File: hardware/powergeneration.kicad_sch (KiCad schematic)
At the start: 36 parts, among them U11 TPS55340PWPR, U5 AOZ1284PI, U6 TL431BIDBZR

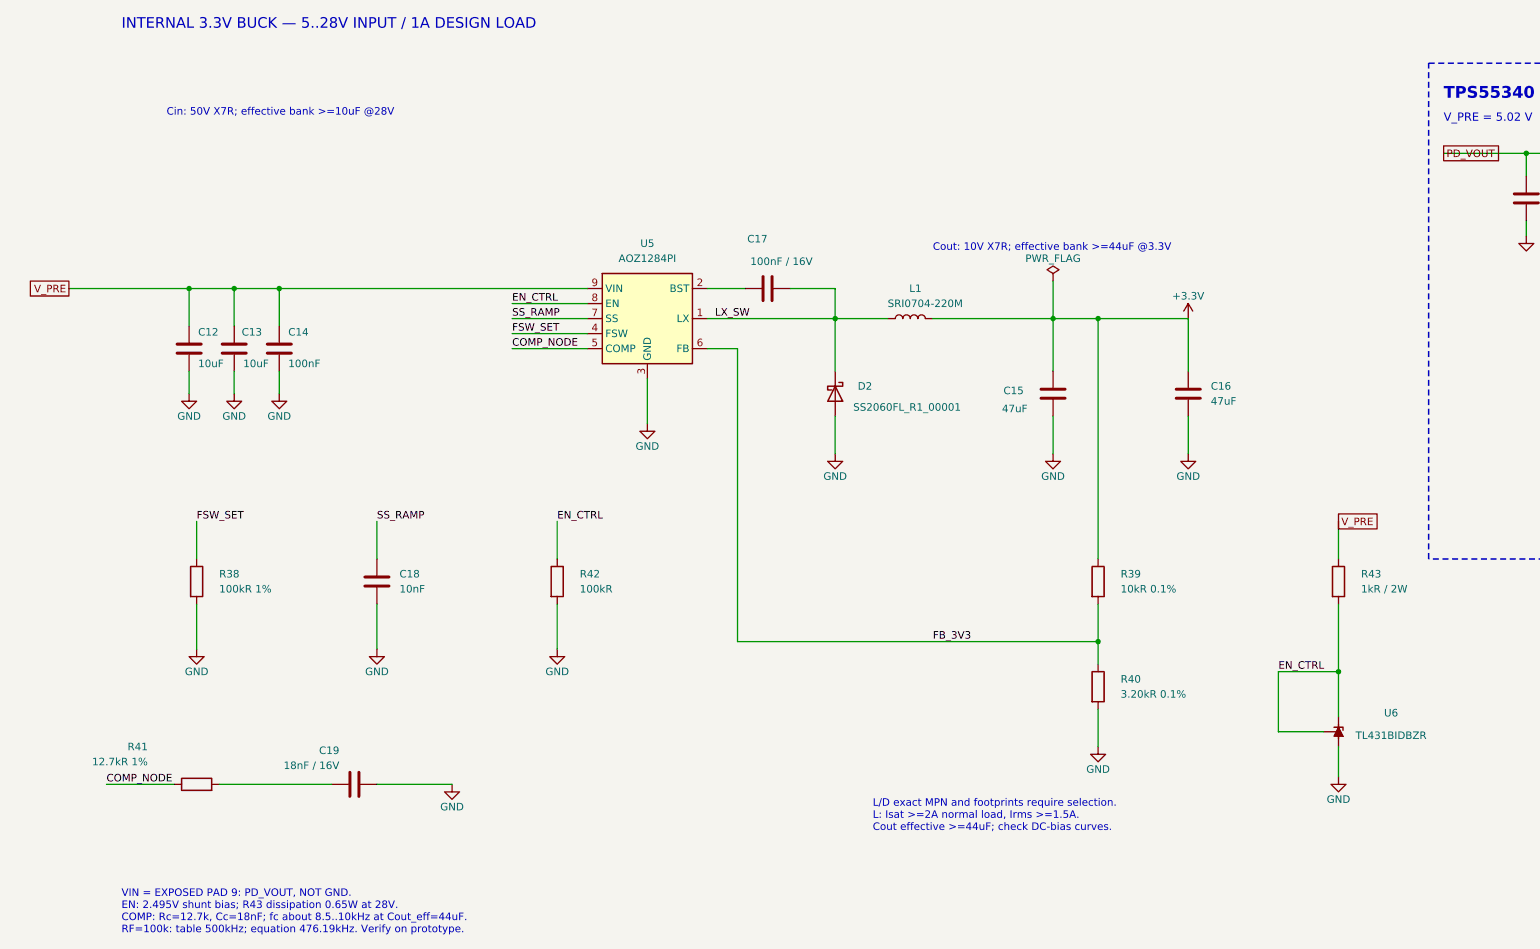
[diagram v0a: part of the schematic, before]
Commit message: powergeneration: AOZ1284 buck bölümünü telle yeniden çiz
Etiketle bağlanan pasifler (EN/TL431, SS, FSW, COMP, FB bölücü) IC
pinlerine gerçek tellerle bağlandı; blok çerçeve ve başlık aldı.
R38-R43 Device:R -> R_Small_US. VIN notu PD_VOUT değil V_PRE olarak
düzeltildi. Netlist değişmedi.

Co-Authored-By: Claude Opus 5 <noreply@anthropic.com>
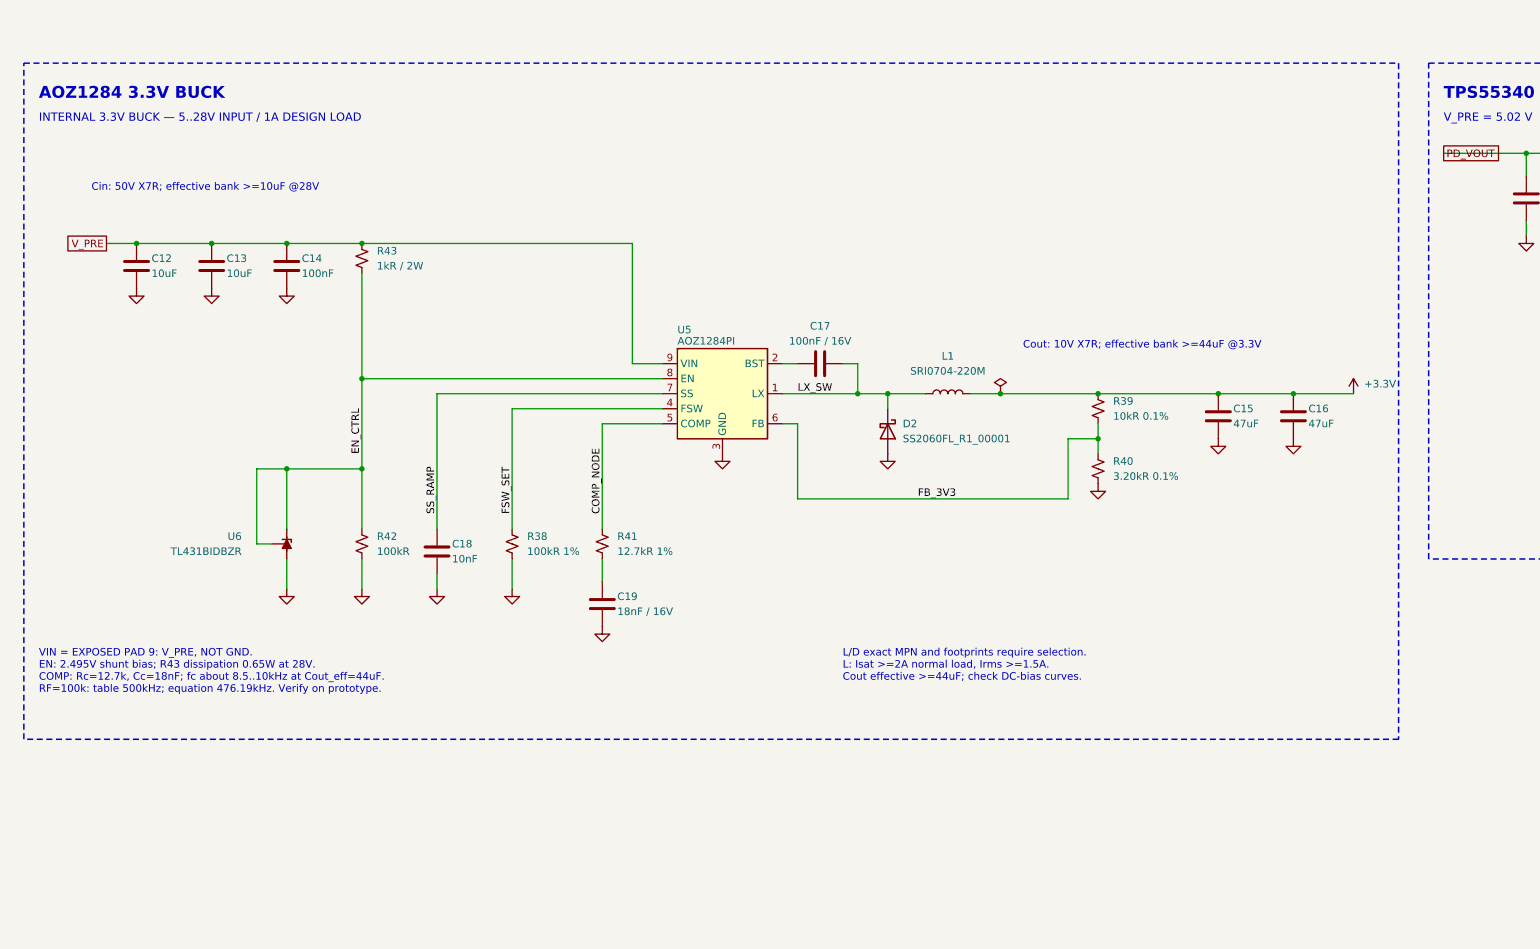
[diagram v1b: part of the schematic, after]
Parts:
- R38, R39, R40, R41, R42, R43: symbol Device:R -> Device:R_Small_US
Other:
- note added: "AOZ1284 3.3V BUCK"
- note added: "VIN = EXPOSED PAD 9: V_PRE, NOT GND. EN: 2.495V shunt bias; R43 dissipation 0.65W at 28V. COMP: Rc=12.7k, Cc=18nF; fc about 8.5..10kHz at Cout_eff=44uF. RF=100k: table 500kHz; equation 476.19kHz. Verify on prototype."
- note removed: "VIN = EXPOSED PAD 9: PD_VOUT, NOT GND. EN: 2.495V shunt bias; R43 dissipation 0.65W at 28V. COMP: Rc=12.7k, Cc=18nF; fc about 8.5..10kHz at Cout_eff=44uF. RF=100k: table 500kHz; equation 476.19kHz. Verify on prototype."
- moved on the sheet: C12, C13, C14, C15, C16, C17, C18, C19, D2, L1, U5, U6
